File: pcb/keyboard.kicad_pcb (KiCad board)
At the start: 2 copper layers, 198.4 x 84.1 mm, 64 parts, among them SW1 SW_Push, U1 ProMicro

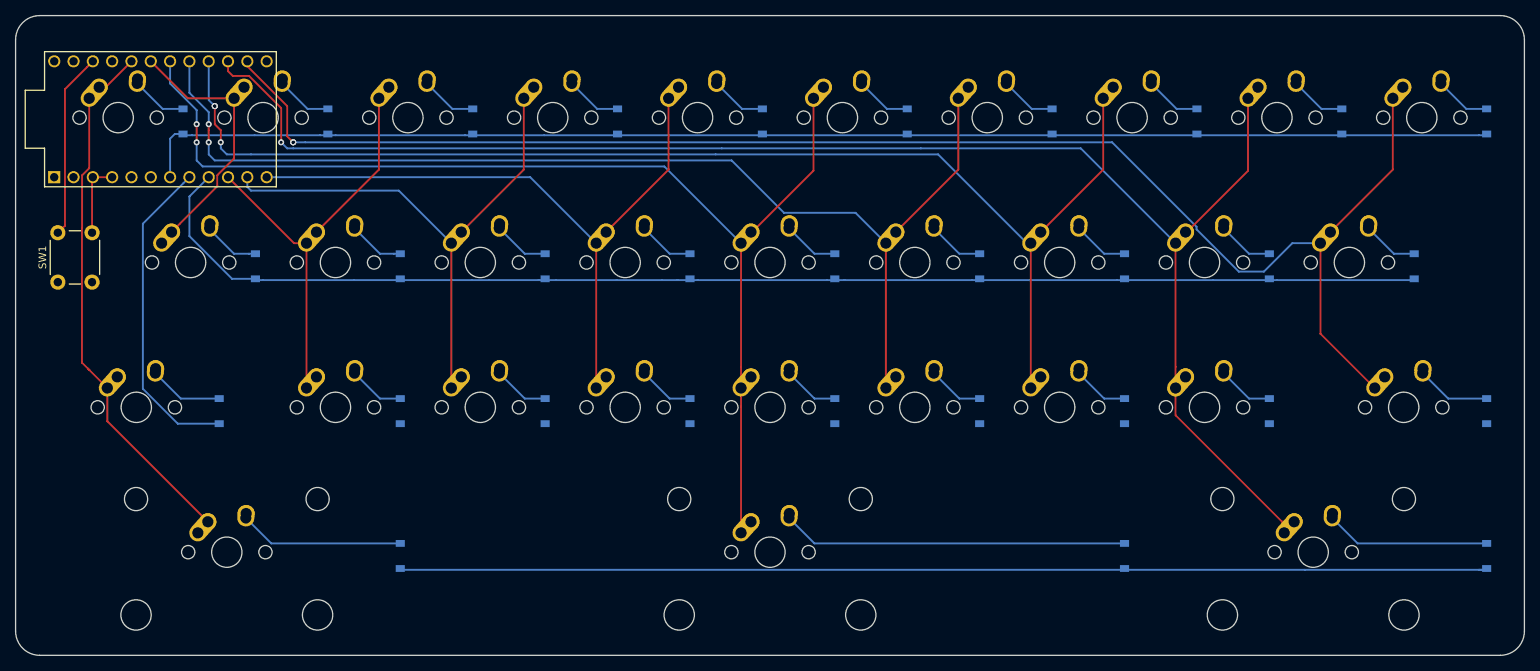
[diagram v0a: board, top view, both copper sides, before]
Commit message: Fixed small errors and added a GND plane
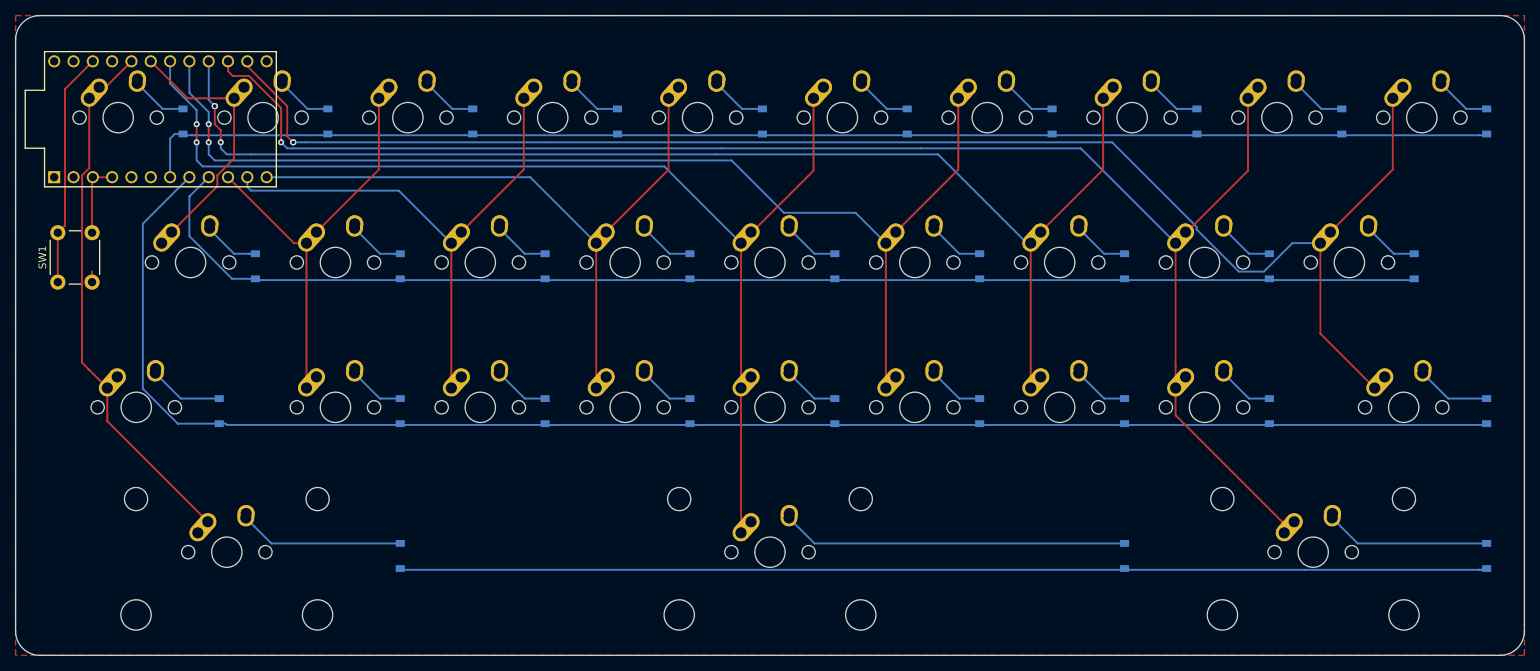
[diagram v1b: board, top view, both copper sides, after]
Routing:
- net row2: track 42.3 -> 208.3 mm
- net rst: track 24.5 -> 31.0 mm
- net GND: track 9.89 -> 11.3 mm
- added copper zone on F.Cu, net GND
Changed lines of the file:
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@@
     (thickness 1.6)
     (drawings 9)
-    (tracks 270)
+    (tracks 291)
     (zones 0)
     (modules 64)
@@
   (segment (start 74.35 91.26125) (end 74.35 84.0625) (width 0.25) (layer F.Cu) (net 1))
   (segment (start 74.45375 83.95875) (end 76.99375 83.95875) (width 0.25) (layer F.Cu) (net 1))
+  (segment (start 74.35 97.76125) (end 74.35 96.347037) (width 0.25) (layer F.Cu) (net 1))
   (segment (start 73.9775 109.305) (end 76.35875 111.68625) (width 0.25) (layer F.Cu) (net 2))
   (segment (start 76.35875 116.06) (end 89.575 129.27625) (width 0.25) (layer F.Cu) (net 2))
@@
   (segment (start 88.10625 81.75625) (end 88.10625 79.375) (width 0.25) (layer B.Cu) (net 7))
   (segment (start 88.10625 79.375) (end 88.10625 79.375) (width 0.25) (layer B.Cu) (net 7))
-  (via (at 88.10625 79.375) (size 0.8) (drill 0.4) (layers F.Cu B.Cu) (net 7) (status 1000000))
+  (via (at 88.10625 79.375) (size 0.8) (drill 0.4) (layers F.Cu B.Cu) (net 7))
   (segment (start 88.10625 79.375) (end 88.10625 76.99375) (width 0.25) (layer F.Cu) (net 7))
   (segment (start 88.10625 76.99375) (end 88.10625 76.99375) (width 0.25) (layer F.Cu) (net 7))
@@
   (segment (start 85.622748 116.37625) (end 81.032499 111.786001) (width 0.25) (layer B.Cu) (net 14))
   (segment (start 91.075 116.37625) (end 85.622748 116.37625) (width 0.25) (layer B.Cu) (net 14))
+  (segment (start 91.075 116.37625) (end 91.925 116.37625) (width 0.25) (layer B.Cu) (net 14))
+  (segment (start 91.925 116.37625) (end 92.093901 116.545151) (width 0.25) (layer B.Cu) (net 14))
+  (segment (start 114.163901 116.545151) (end 115.229849 116.545151) (width 0.25) (layer B.Cu) (net 14))
+  (segment (start 92.093901 116.545151) (end 114.163901 116.545151) (width 0.25) (layer B.Cu) (net 14))
+  (segment (start 230.206401 116.545151) (end 257.311099 116.545151) (width 0.25) (layer B.Cu) (net 14))
+  (segment (start 230.206401 116.545151) (end 229.529849 116.545151) (width 0.25) (layer B.Cu) (net 14))
+  (segment (start 173.056401 116.545151) (end 172.379849 116.545151) (width 0.25) (layer B.Cu) (net 14))
+  (segment (start 192.106401 116.545151) (end 190.636099 116.545151) (width 0.25) (layer B.Cu) (net 14))
+  (segment (start 173.056401 116.545151) (end 190.636099 116.545151) (width 0.25) (layer B.Cu) (net 14))
+  (segment (start 211.156401 116.545151) (end 209.686099 116.545151) (width 0.25) (layer B.Cu) (net 14))
+  (segment (start 192.106401 116.545151) (end 209.686099 116.545151) (width 0.25) (layer B.Cu) (net 14))
+  (segment (start 134.956401 116.545151) (end 151.968599 116.545151) (width 0.25) (layer B.Cu) (net 14))
+  (segment (start 211.156401 116.545151) (end 228.736099 116.545151) (width 0.25) (layer B.Cu) (net 14))
+  (segment (start 154.006401 116.545151) (end 172.379849 116.545151) (width 0.25) (layer B.Cu) (net 14))
+  (segment (start 154.006401 116.545151) (end 153.329849 116.545151) (width 0.25) (layer B.Cu) (net 14))
+  (segment (start 151.968599 116.545151) (end 153.057651 116.545151) (width 0.25) (layer B.Cu) (net 14))
+  (segment (start 134.956401 116.545151) (end 134.279849 116.545151) (width 0.25) (layer B.Cu) (net 14))
+  (segment (start 133.768599 116.545151) (end 133.9375 116.37625) (width 0.25) (layer B.Cu) (net 14))
+  (segment (start 114.163901 116.545151) (end 133.768599 116.545151) (width 0.25) (layer B.Cu) (net 14))
   (segment (start 256.743599 135.595151) (end 257.826401 135.595151) (width 0.25) (layer B.Cu) (net 15))
   (segment (start 209.968599 135.595151) (end 210.1375 135.42625) (width 0.25) (layer B.Cu) (net 15))
@@
   (segment (start 70.788749 72.383751) (end 73.653751 69.518749) (width 0.25) (layer F.Cu) (net 54))
   (segment (start 69.87 91.26125) (end 70.788749 90.342501) (width 0.25) (layer F.Cu) (net 54))
+  (segment (start 69.85 97.76125) (end 69.85 91.26125) (width 0.25) (layer F.Cu) (net 54))
+  (zone (net 1) (net_name GND) (layer F.Cu) (hatch edge 0.508)
+    (connect_pads (clearance 0.508))
+    (min_thickness 0.254)
+    (fill yes (arc_segments 32) (thermal_gap 0.508) (thermal_bridge_width 0.508))
+    (polygon
+      (pts
+        (xy 262.73125 62.70625) (xy 262.73125 146.84375) (xy 64.29375 146.84375) (xy 64.29375 62.70625)
+      )
+    )
+  )
 )
